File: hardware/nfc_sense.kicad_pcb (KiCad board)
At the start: 4 copper layers, 18.6 x 43.1 mm, 25 parts, among them U1 TMP117AIDRVR, U2 RF430CL330HIRGTR‎, U3 ATtiny1626-MFR

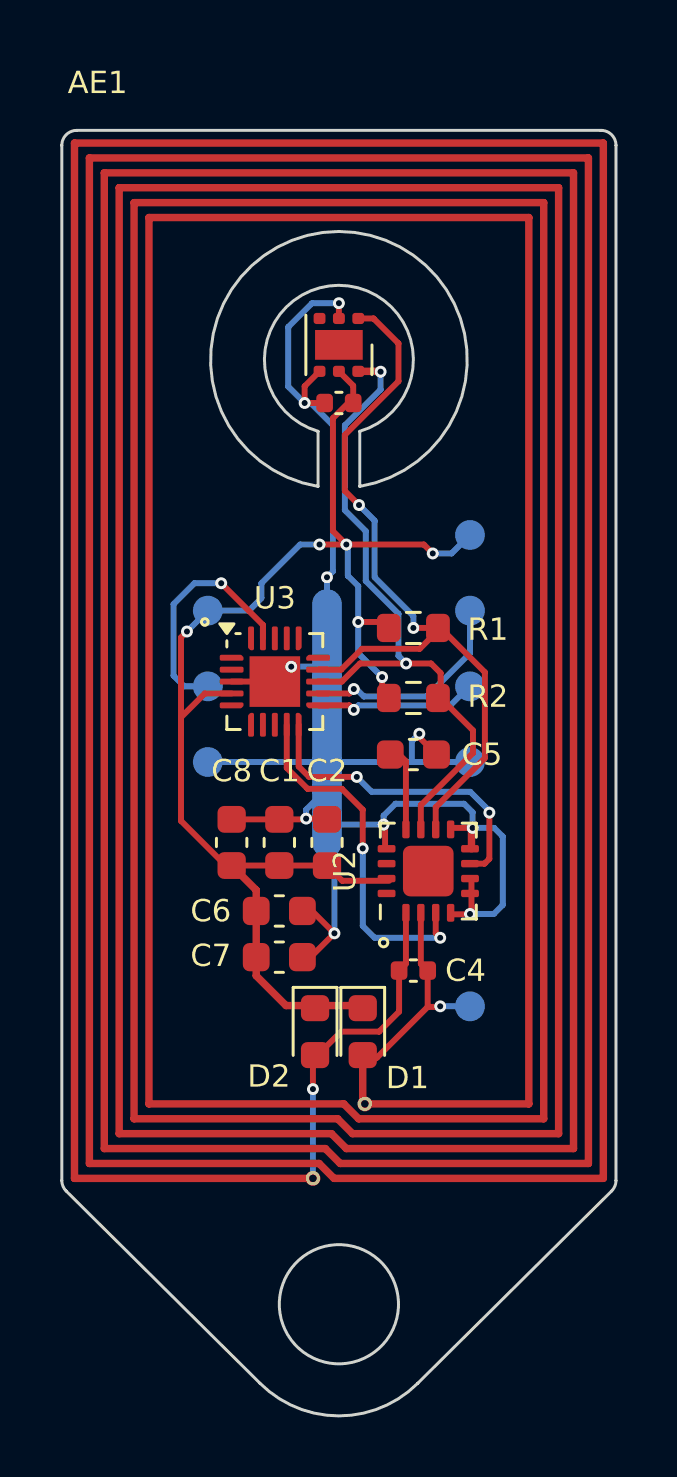
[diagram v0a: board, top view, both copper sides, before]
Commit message: update design to prevent manufacturing errors
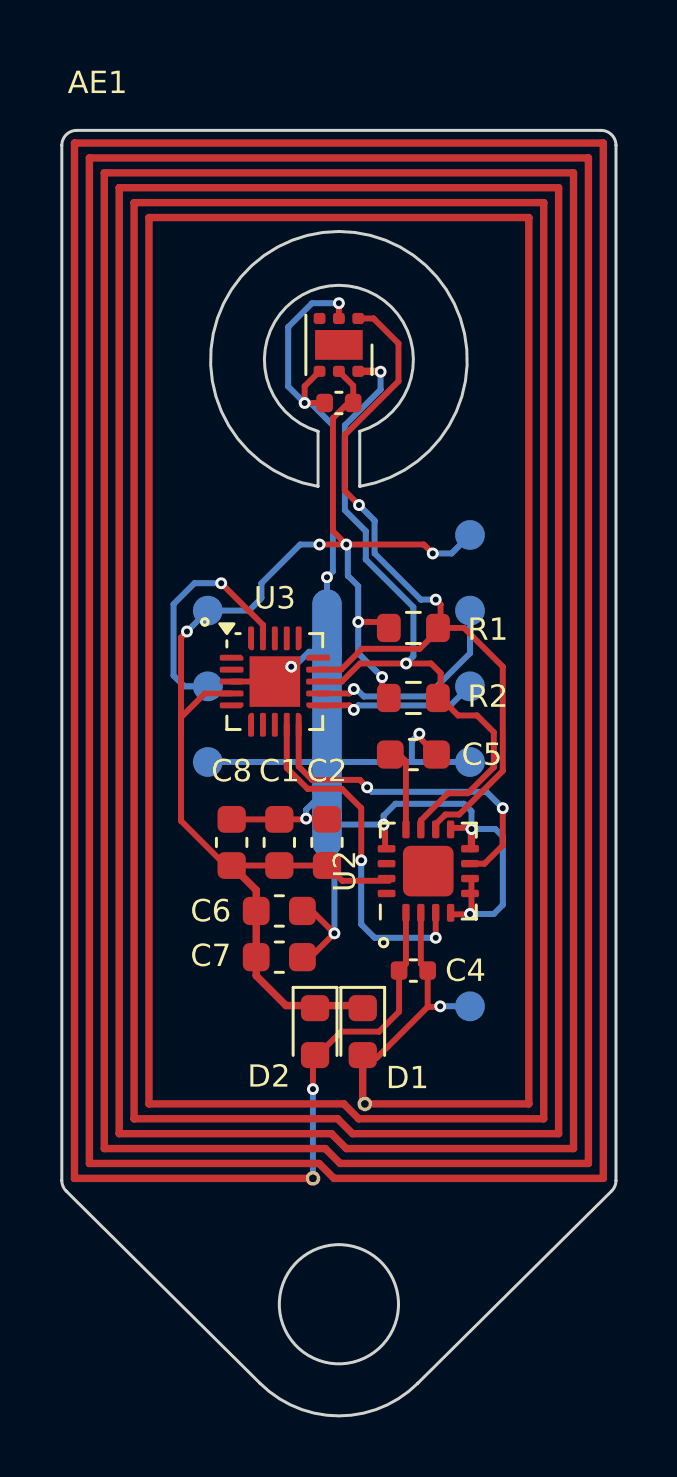
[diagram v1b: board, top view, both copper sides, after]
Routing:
- net SDA: track 22.8 -> 24.4 mm
- net SCL: track 26.6 -> 27.5 mm
- net RF430_INT: track 10.7 -> 11.4 mm
- net GND: track 62.0 -> 62.6 mm

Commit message: update traces for better manufacturing
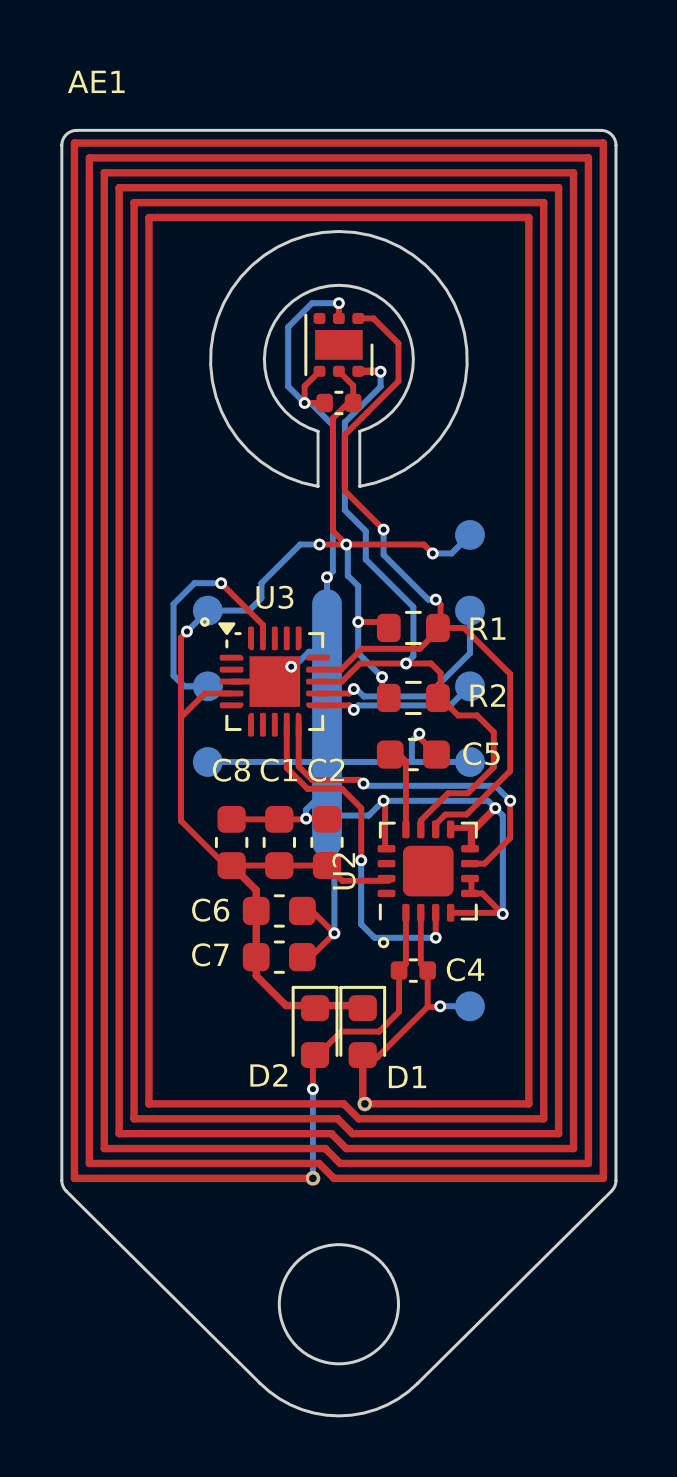
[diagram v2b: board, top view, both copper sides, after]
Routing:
- net GND: track 62.6 -> 66.1 mm
- net RF430_INT: track 11.4 -> 11.9 mm

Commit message: update DRC for 0.8 mm
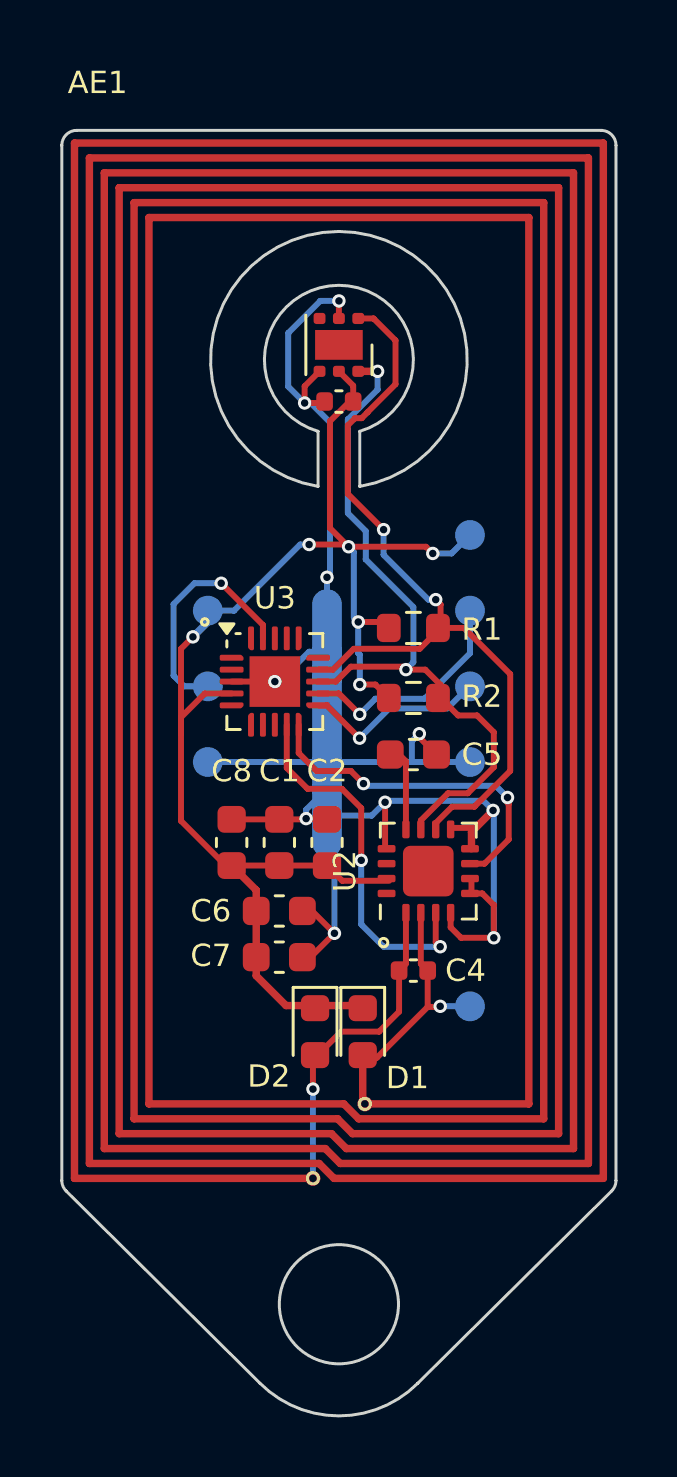
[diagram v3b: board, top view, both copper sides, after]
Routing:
- net GND: track 66.1 -> 68.1 mm
- net RX: track 5.50 -> 6.28 mm
- net RF430_RST: track 11.9 -> 12.5 mm

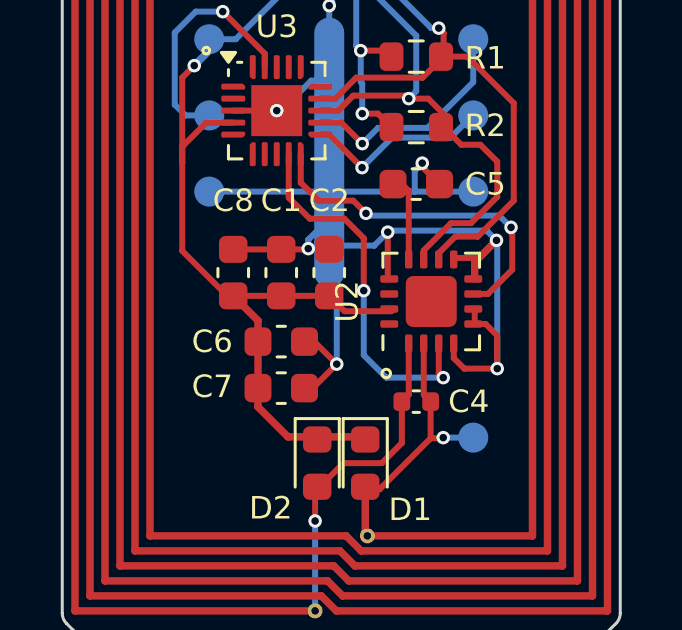
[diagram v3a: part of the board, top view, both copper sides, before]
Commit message: update RF430 footprint
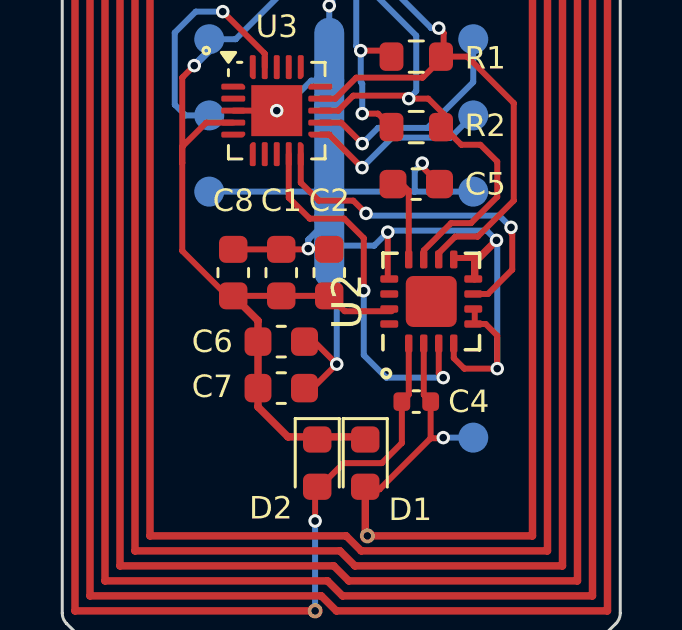
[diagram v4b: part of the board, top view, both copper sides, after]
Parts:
- U2: footprint unsurv_offline_pcb_footprints:RF430_3x3mm_regular -> unsurv_offline_pcb_footprints:RF430_3x3mm_regular_noBCu
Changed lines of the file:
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@@
 		)
 	)
-	(footprint "unsurv_offline_pcb_footprints:RF430_3x3mm_regular"
+	(footprint "unsurv_offline_pcb_footprints:RF430_3x3mm_regular_noBCu"
 		(layer "F.Cu")
 		(at 132.5 56.36179 90)
@@
 		(property "Reference" "U2"
 			(at 0 -2.8 90)
-			(unlocked yes)
-			(layer "F.SilkS")
-			(effects
-				(font
-					(size 0.75 0.75)
-					(thickness 0.125)
+			(layer "F.SilkS")
+			(effects
+				(font
+					(size 1 1)
+					(thickness 0.15)
 				)
 			)
@@
 		(property "Value" "RF430CL330HIRGTR‎"
 			(at 0 2.8 90)
-			(unlocked yes)
 			(layer "F.Fab")
 			(effects
@@
 			)
 		)
-		(property "Footprint" "unsurv_offline_pcb_footprints:RF430_3x3mm_regular"
+		(property "Footprint" "unsurv_offline_pcb_footprints:RF430_3x3mm_regular_noBCu"
 			(at 0 0 90)
 			(layer "F.Fab")
@@
 			(end 1.61 -1.135)
 			(stroke
-				(width 0.1)
+				(width 0.12)
 				(type solid)
 			)
@@
 			(end 1.61 -1.61)
 			(stroke
-				(width 0.1)
+				(width 0.12)
 				(type solid)
 			)
@@
 			(end -1.61 -1.61)
 			(stroke
-				(width 0.1)
+				(width 0.12)
 				(type solid)
 			)
@@
 			(end 1.61 1.135)
 			(stroke
-				(width 0.1)
+				(width 0.12)
 				(type solid)
 			)
@@
 			(end 1.61 1.61)
 			(stroke
-				(width 0.1)
+				(width 0.12)
 				(type solid)
 			)
@@
 			(end -1.61 1.61)
 			(stroke
-				(width 0.1)
+				(width 0.12)
 				(type solid)
 			)
@@
 			(end -1.61 1.135)
 			(stroke
-				(width 0.1)
+				(width 0.12)
 				(type solid)
 			)
@@
 			(end -2.5 -1.4)
 			(stroke
-				(width 0.1)
+				(width 0.12)
 				(type solid)
 			)
@@
 		(fp_text user "${REFERENCE}"
 			(at 0 0 90)
-			(unlocked yes)
-			(layer "F.Fab")
-			(effects
-				(font
-					(size 1 1)
-					(thickness 0.15)
+			(layer "F.Fab")
+			(effects
+				(font
+					(size 0.75 0.75)
+					(thickness 0.11)
 				)
 			)
@@
 		)
 		(pad "2" smd roundrect
-			(at -1.4 -0.25 90)
+			(at -1.4 -0.25 270)
 			(size 0.6 0.25)
 			(layers "F.Cu" "F.Paste" "F.Mask")
@@
 		)
 		(pad "3" smd roundrect
-			(at -1.4 0.25 90)
+			(at -1.4 0.25 270)
 			(size 0.6 0.25)
 			(layers "F.Cu" "F.Paste" "F.Mask")
@@
 		)
 		(pad "4" smd roundrect
-			(at -1.4 0.75 90)
+			(at -1.4 0.75 270)
 			(size 0.6 0.25)
 			(layers "F.Cu" "F.Paste" "F.Mask")
@@
 		)
 		(pad "5" smd roundrect
-			(at -0.75 1.4 90)
-			(size 0.25 0.6)
+			(at -0.75 1.4 180)
+			(size 0.6 0.25)
 			(layers "F.Cu" "F.Paste" "F.Mask")
 			(roundrect_rratio 0.25)
@@
 		)
 		(pad "6" smd roundrect
-			(at -0.25 1.4 90)
-			(size 0.25 0.6)
+			(at -0.25 1.4 180)
+			(size 0.6 0.25)
 			(layers "F.Cu" "F.Paste" "F.Mask")
 			(roundrect_rratio 0.25)
@@
 		)
 		(pad "7" smd roundrect
-			(at 0.25 1.4 90)
-			(size 0.25 0.6)
+			(at 0.25 1.4 180)
+			(size 0.6 0.25)
 			(layers "F.Cu" "F.Paste" "F.Mask")
 			(roundrect_rratio 0.25)
@@
 		)
 		(pad "8" smd roundrect
-			(at 0.75 1.4 90)
-			(size 0.25 0.6)
+			(at 0.75 1.4 180)
+			(size 0.6 0.25)
 			(layers "F.Cu" "F.Paste" "F.Mask")
 			(roundrect_rratio 0.25)
@@
 		)
 		(pad "9" smd roundrect
-			(at 1.4 0.75 90)
+			(at 1.4 0.75 270)
 			(size 0.6 0.25)
 			(layers "F.Cu" "F.Paste" "F.Mask")
@@
 		)
 		(pad "13" smd roundrect
-			(at 0.75 -1.4 90)
-			(size 0.25 0.6)
+			(at 0.75 -1.4)
+			(size 0.6 0.25)
 			(layers "F.Cu" "F.Paste" "F.Mask")
 			(roundrect_rratio 0.25)
@@
 		)
 		(pad "14" smd roundrect
-			(at 0.25 -1.4 90)
-			(size 0.25 0.6)
+			(at 0.25 -1.4 180)
+			(size 0.6 0.25)
 			(layers "F.Cu" "F.Paste" "F.Mask")
 			(roundrect_rratio 0.25)
@@
 		)
 		(pad "15" smd roundrect
-			(at -0.25 -1.4 90)
-			(size 0.25 0.6)
+			(at -0.25 -1.4 180)
+			(size 0.6 0.25)
 			(layers "F.Cu" "F.Paste" "F.Mask")
 			(roundrect_rratio 0.25)
@@
 		)
 		(pad "16" smd roundrect
-			(at -0.75 -1.4 90)
-			(size 0.25 0.6)
-			(layers "F.Cu" "F.Paste" "F.Mask")
-			(roundrect_rratio 0.25)
+			(at -0.75 -1.4 180)
+			(size 0.6 0.25)
+			(layers "F.Cu" "F.Paste" "F.Mask")
+			(roundrect_rratio 0.25)

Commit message: update PCBs
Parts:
- moved C6 1.60 mm to (127.5, 59.3)
- moved C7 1.55 mm to (127.5, 57.7)
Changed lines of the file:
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@@
 	(footprint "Capacitor_SMD:C_0603_1608Metric"
 		(layer "F.Cu")
-		(at 127.5 57.7)
+		(at 127.5 59.3)
 		(descr "Capacitor SMD 0603 (1608 Metric), square (rectangular) end terminal, IPC_7351 nominal, (Body size source: IPC-SM-782 page 76, https://www.pcb-3d.com/wordpress/wp-content/uploads/ipc-sm-782a_amendment_1_and_2.pdf), generated with kicad-footprint-generator")
 		(tags "capacitor")
@@
 	(footprint "Capacitor_SMD:C_0603_1608Metric"
 		(layer "F.Cu")
-		(at 127.5 59.25)
+		(at 127.5 57.7)
 		(descr "Capacitor SMD 0603 (1608 Metric), square (rectangular) end terminal, IPC_7351 nominal, (Body size source: IPC-SM-782 page 76, https://www.pcb-3d.com/wordpress/wp-content/uploads/ipc-sm-782a_amendment_1_and_2.pdf), generated with kicad-footprint-generator")
 		(tags "capacitor")
